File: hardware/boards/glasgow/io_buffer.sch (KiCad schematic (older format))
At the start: 62 parts, among them J2 Conn_02x10_Odd_Even, J6 Conn_01x08, J7 Conn_01x08, U10 DAC081C081CIMK, U11 TPS73101DBV, U16 SN74LVC1T45DRL, U17 SN74LVC1T45DRL, U18 SN74LVC1T45DRL, U19 PCA6408APW, U19 SN74LVC1T45DRL, U20 SN74LVC1T45DRL, U21 INA233, U21 SN74LVC1T45DRL, U33 MG2040, U5 SN74LVC1T45DRL, U6 SN74LVC1T45DRL

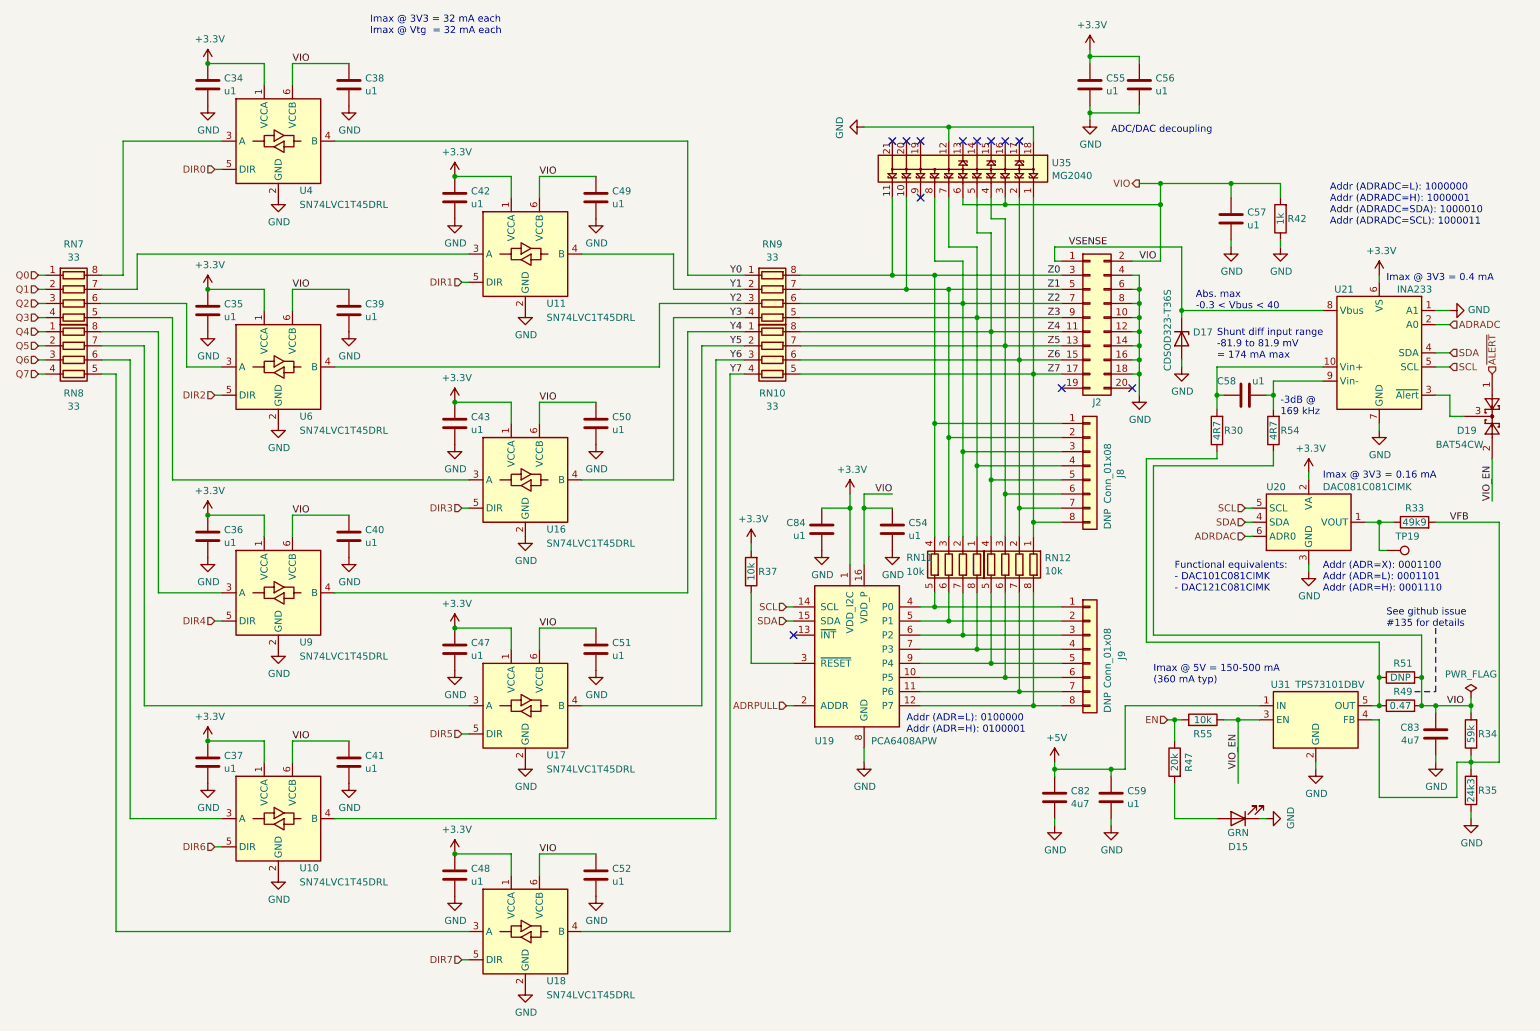
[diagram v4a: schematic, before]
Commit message: revC2: roundrect and fixed 3d model for USB-C socket
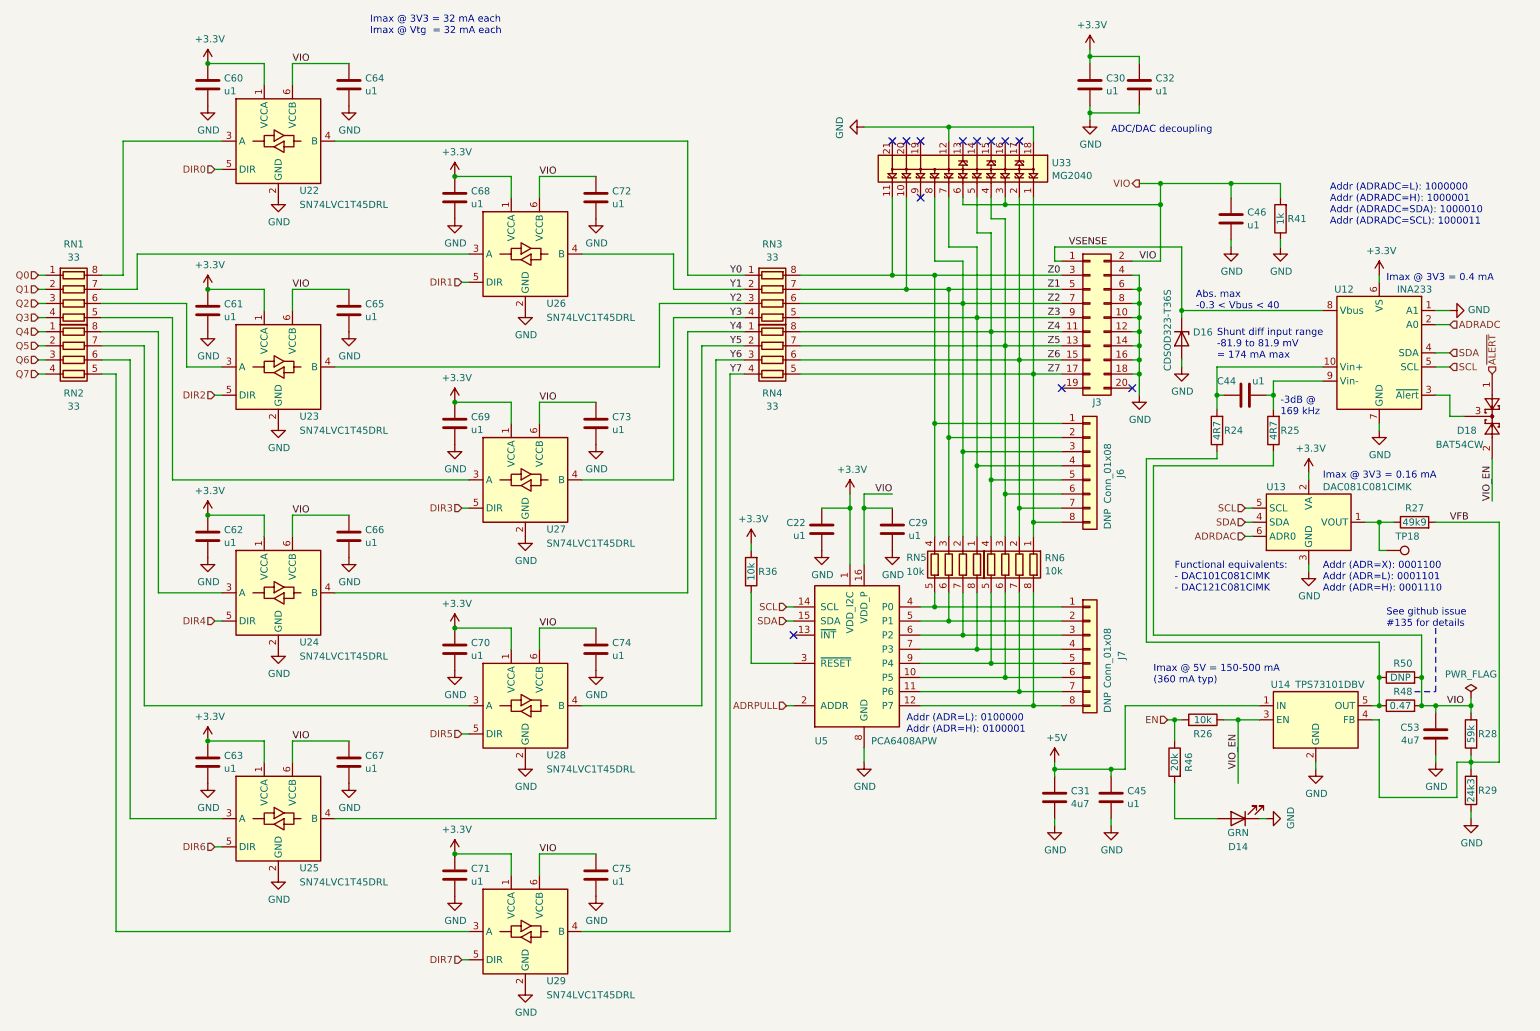
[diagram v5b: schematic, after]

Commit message: revC2: add symbol & footprint for new TVS diode array SP3012-06UTG
TODO: 3D model is just a placeholder, to be replaced with the correct one
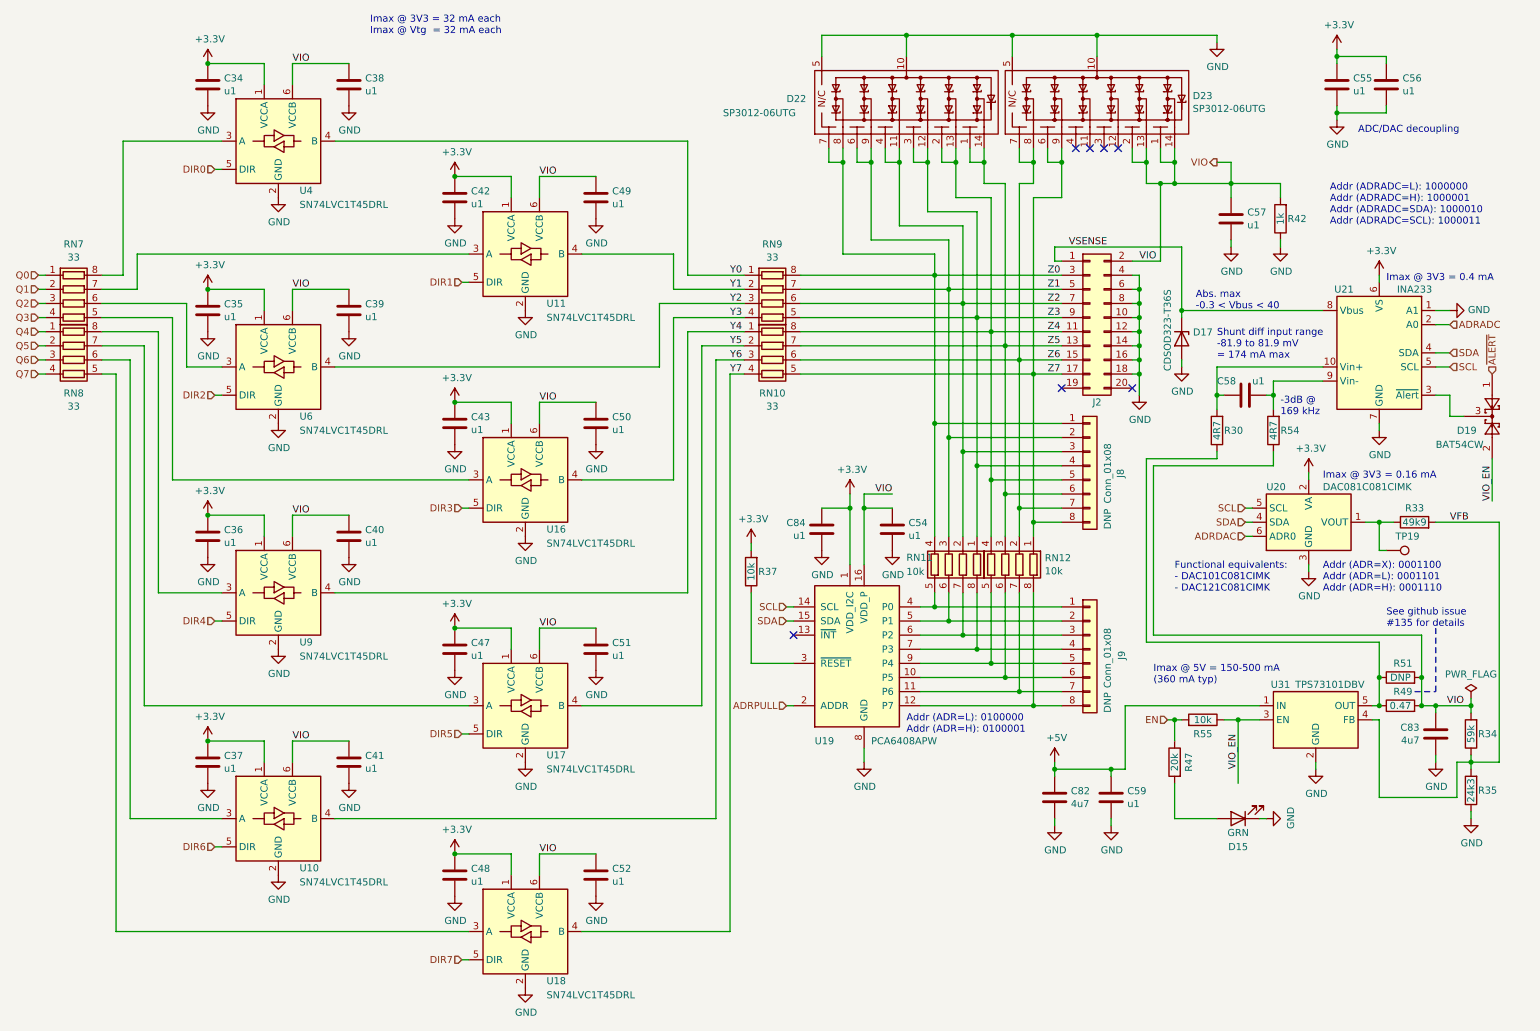
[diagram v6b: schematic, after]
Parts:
- removed U33: MG2040, Glasgow:UDFN-18_5.5x1.5mm_P0.5mm, symbol Glasgow:MG2040
- added D22, D23: SP3012-06UTG, Glasgow:UDFN-14_3.5x1.35mm_P0.5mm, symbol Glasgow:SP3012-06UTG
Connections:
- net GND: now also D22.10 (GND), D22.5 (N/C), D23.10 (GND), D23.5 (N/C)
- net VIO: now also D23.1 (N/C), D23.13 (Ch2), D23.14 (Ch1), D23.2 (N/C)
- net Z0: now also D22.7 (N/C), D22.8 (Ch6)
- net Z1: now also D22.6 (N/C), D22.9 (Ch5)
- net Z2: now also D22.11 (Ch4), D22.4 (N/C)
- net Z3: now also D22.12 (Ch3), D22.3 (N/C)
- net Z4: now also D22.13 (Ch2), D22.2 (N/C)
- net Z5: now also D22.1 (N/C), D22.14 (Ch1)
- net Z6: now also D23.7 (N/C), D23.8 (Ch6)
- net Z7: now also D23.6 (N/C), D23.9 (Ch5)
- no-connect marks 12 -> 7
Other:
- moved on the sheet: C55, C56

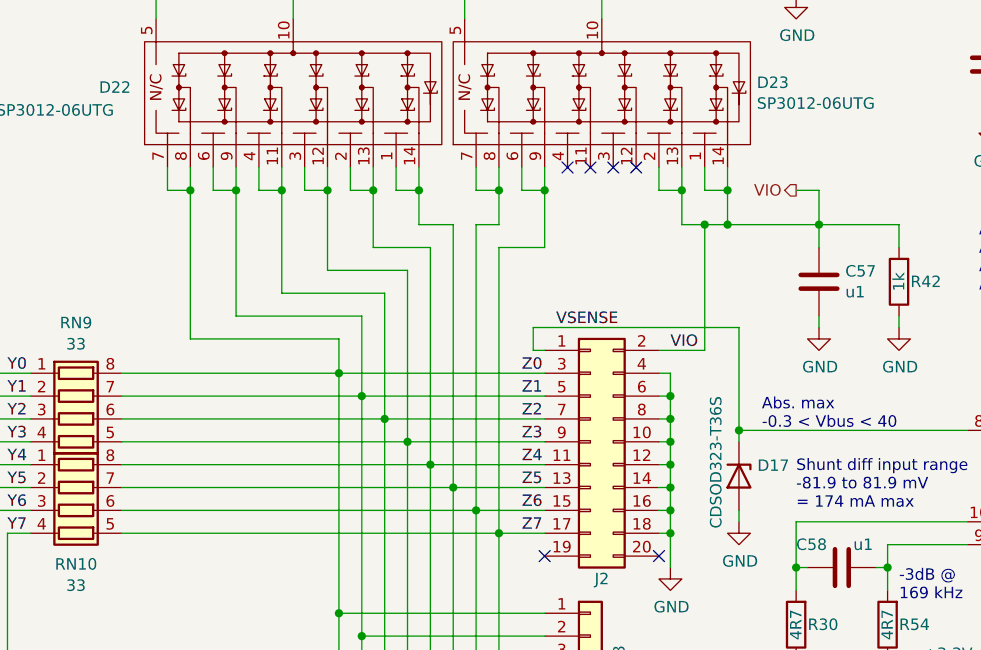
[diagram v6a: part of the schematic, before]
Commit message: revC2: place new TVS diodes for port A
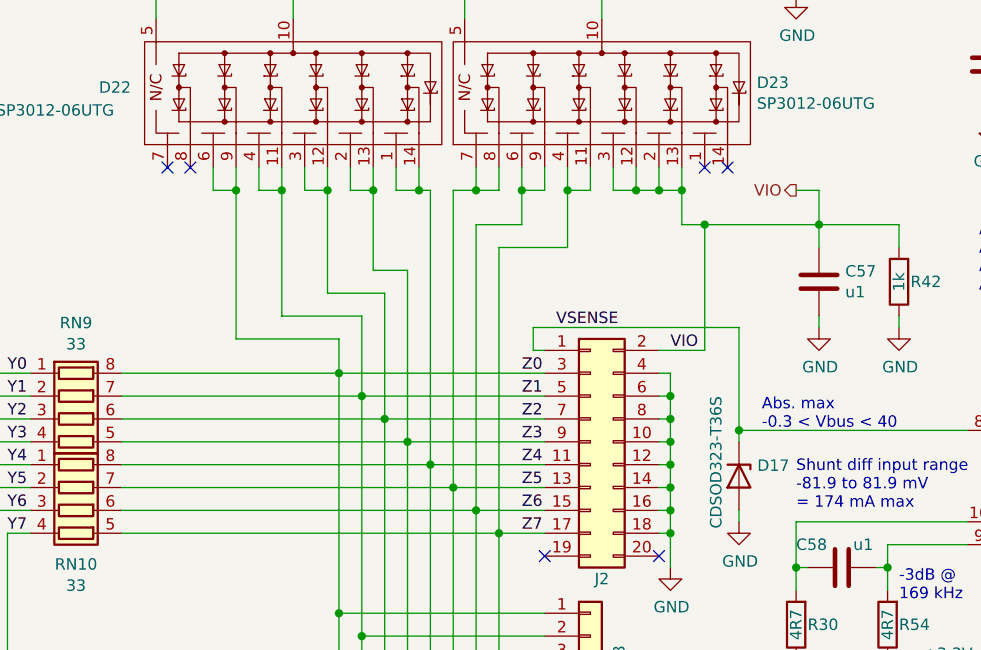
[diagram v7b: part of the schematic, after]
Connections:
- net VIO: now also D23.12 (Ch3), D23.3 (N/C); no longer D23.1 (N/C), D23.14 (Ch1)
- net Z0: now also D22.6 (N/C), D22.9 (Ch5); no longer D22.7 (N/C), D22.8 (Ch6)
- net Z1: now also D22.11 (Ch4), D22.4 (N/C); no longer D22.6 (N/C), D22.9 (Ch5)
- net Z2: now also D22.12 (Ch3), D22.3 (N/C); no longer D22.11 (Ch4), D22.4 (N/C)
- net Z3: now also D22.13 (Ch2), D22.2 (N/C); no longer D22.12 (Ch3), D22.3 (N/C)
- net Z4: now also D22.1 (N/C), D22.14 (Ch1); no longer D22.13 (Ch2), D22.2 (N/C)
- net Z5: now also D23.7 (N/C), D23.8 (Ch6); no longer D22.1 (N/C), D22.14 (Ch1)
- net Z6: now also D23.6 (N/C), D23.9 (Ch5); no longer D23.7 (N/C), D23.8 (Ch6)
- net Z7: now also D23.11 (Ch4), D23.4 (N/C); no longer D23.6 (N/C), D23.9 (Ch5)
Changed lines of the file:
@@
 Wire Wire Line
 	9250 1850 9250 1750
-Wire Wire Line
-	9250 1750 8850 1750
 Text Notes 6950 5650 0    50   ~ 0
 Addr (ADR=L): 0100000\nAddr (ADR=H): 0100001
@@
 Wire Wire Line
 	7850 3100 7850 4150
-Wire Wire Line
-	7850 1850 7850 3100
 NoConn ~ 6150 4950
 $Comp
@@
 	6200 2500 7250 2500
 Wire Wire Line
-	7850 1850 8050 1850
-Wire Wire Line
-	8050 1850 8050 1600
-Wire Wire Line
-	7750 1750 7850 1750
-Wire Wire Line
-	7850 1750 7850 1600
-Wire Wire Line
-	7750 1750 7750 3000
-Wire Wire Line
-	7650 1750 7500 1750
-Wire Wire Line
-	7500 1750 7500 1600
-Wire Wire Line
-	7650 1750 7650 2900
-Wire Wire Line
-	7550 1850 7300 1850
-Wire Wire Line
-	7300 1850 7300 1600
-Wire Wire Line
-	7550 1850 7550 2800
-Wire Wire Line
-	7450 1950 7100 1950
-Wire Wire Line
-	7100 1950 7100 1600
-Wire Wire Line
 	7450 1950 7450 2700
 Wire Wire Line
-	7350 2050 6900 2050
-Wire Wire Line
-	6900 2050 6900 1600
+	7350 2050 7100 2050
 Wire Wire Line
 	7350 2050 7350 2600
@@
 	7250 2500 7250 2150
 Wire Wire Line
-	7250 2150 6700 2150
-Wire Wire Line
-	6700 2150 6700 1600
-Wire Wire Line
-	7150 2250 6500 2250
-Wire Wire Line
-	6500 2250 6500 1600
+	7250 2150 6900 2150
+Wire Wire Line
+	7150 2250 6700 2250
 Wire Wire Line
 	7150 2250 7150 2400
@@
 Wire Wire Line
 	9250 1600 9250 1750
-Wire Wire Line
-	8850 1500 8850 1600
-Connection ~ 8850 1750
-Wire Wire Line
-	8850 1750 8750 1750
 Wire Wire Line
 	8750 1750 8650 1750
@@
 Connection ~ 8750 1750
 Wire Wire Line
-	6500 1600 6400 1600
-Wire Wire Line
-	6400 1600 6400 1500
-Connection ~ 6500 1600
-Wire Wire Line
-	6500 1600 6500 1500
-Wire Wire Line
-	6700 1600 6600 1600
-Wire Wire Line
-	6600 1600 6600 1500
-Connection ~ 6700 1600
-Wire Wire Line
-	6700 1600 6700 1500
-Wire Wire Line
-	6900 1600 6800 1600
-Wire Wire Line
-	6800 1600 6800 1500
-Connection ~ 6900 1600
-Wire Wire Line
-	6900 1600 6900 1500
-Wire Wire Line
-	7100 1600 7000 1600
-Wire Wire Line
-	7000 1600 7000 1500
-Connection ~ 7100 1600
-Wire Wire Line
-	7100 1600 7100 1500
-Wire Wire Line
-	7300 1600 7200 1600
-Wire Wire Line
-	7200 1600 7200 1500
-Connection ~ 7300 1600
-Wire Wire Line
-	7300 1600 7300 1500
-Wire Wire Line
-	7500 1600 7400 1600
-Wire Wire Line
-	7400 1600 7400 1500
-Connection ~ 7500 1600
-Wire Wire Line
-	7500 1600 7500 1500
-Wire Wire Line
-	7850 1600 7750 1600
-Wire Wire Line
-	7750 1600 7750 1500
-Connection ~ 7850 1600
-Wire Wire Line
-	7850 1600 7850 1500
-Wire Wire Line
-	8050 1600 7950 1600
-Wire Wire Line
-	7950 1600 7950 1500
-Connection ~ 8050 1600
-Wire Wire Line
-	8050 1600 8050 1500
-Wire Wire Line
 	8650 1600 8550 1600
 Wire Wire Line
@@
 Wire Wire Line
 	8650 1600 8650 1500
-Wire Wire Line
-	8850 1600 8750 1600
-Wire Wire Line
-	8750 1600 8750 1500
-Connection ~ 8850 1600
-Wire Wire Line
-	8850 1600 8850 1750
 $Comp
 L power:GND #PWR0141
@@
 	6350 700  6350 850
 Connection ~ 6950 700
-NoConn ~ 8150 1500
-NoConn ~ 8250 1500
-NoConn ~ 8350 1500
-NoConn ~ 8450 1500
 $Comp
 L Glasgow:SP3012-06UTG D23
@@
 	-1   0    0    1
 $EndComp
+Wire Wire Line
+	7850 1850 7850 3100
+Wire Wire Line
+	7750 1750 7750 3000
+Wire Wire Line
+	8750 1750 9250 1750
+Wire Wire Line
+	8550 1600 8450 1600
+Wire Wire Line
+	8450 1600 8450 1500
+Connection ~ 8550 1600
+Wire Wire Line
+	8450 1600 8350 1600
+Wire Wire Line
+	8350 1600 8350 1500
+Connection ~ 8450 1600
+NoConn ~ 8750 1500
+NoConn ~ 8850 1500
+Wire Wire Line
+	7650 1600 7750 1600
+Wire Wire Line
+	7750 1600 7750 1500
+Wire Wire Line
+	7650 1600 7650 2900
+Wire Wire Line
+	7750 1600 7850 1600
+Wire Wire Line
+	7850 1600 7850 1500
+Connection ~ 7750 1600
+Wire Wire Line
+	7750 1750 7950 1750
+Wire Wire Line
+	7950 1750 7950 1600
+Wire Wire Line
+	7950 1600 8050 1600
+Wire Wire Line
+	8050 1600 8050 1500
+Connection ~ 7950 1600
+Wire Wire Line
+	7950 1600 7950 1500
+Wire Wire Line
+	7850 1850 8150 1850
+Wire Wire Line
+	8150 1850 8150 1600
+Wire Wire Line
+	8150 1600 8250 1600
+Wire Wire Line
+	8250 1600 8250 1500
+Connection ~ 8150 1600
+Wire Wire Line
+	8150 1600 8150 1500
+Wire Wire Line
+	7550 1600 7500 1600
+Wire Wire Line
+	7400 1600 7400 1500
+Wire Wire Line
+	7550 1600 7550 2800
+Wire Wire Line
+	7500 1600 7500 1500
+Connection ~ 7500 1600
+Wire Wire Line
+	7500 1600 7400 1600
+Wire Wire Line
+	7450 1950 7300 1950
+Wire Wire Line
+	7300 1950 7300 1600
+Wire Wire Line
+	7300 1600 7200 1600
+Wire Wire Line
+	7200 1600 7200 1500
+Connection ~ 7300 1600
+Wire Wire Line
+	7300 1600 7300 1500
+Wire Wire Line
+	7100 1500 7100 1600
+Wire Wire Line
+	7100 1600 7000 1600
+Wire Wire Line
+	7000 1600 7000 1500
+Connection ~ 7100 1600
+Wire Wire Line
+	7100 1600 7100 2050
+Wire Wire Line
+	6900 1500 6900 1600
+Wire Wire Line
+	6900 1600 6800 1600
+Wire Wire Line
+	6800 1600 6800 1500
+Connection ~ 6900 1600
+Wire Wire Line
+	6900 1600 6900 2150
 $Comp
 L Glasgow:SP3012-06UTG D22
@@
 	-1   0    0    1
 $EndComp
+Wire Wire Line
+	6700 1500 6700 1600
+Wire Wire Line
+	6700 1600 6600 1600
+Wire Wire Line
+	6600 1600 6600 1500
+Connection ~ 6700 1600
+Wire Wire Line
+	6700 1600 6700 2250
+NoConn ~ 6500 1500
+NoConn ~ 6400 1500
 $EndSCHEMATC
